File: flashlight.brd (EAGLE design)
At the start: 33.2 x 17.8 mm, 2 parts, among them IC1 AMC7135SOT-89

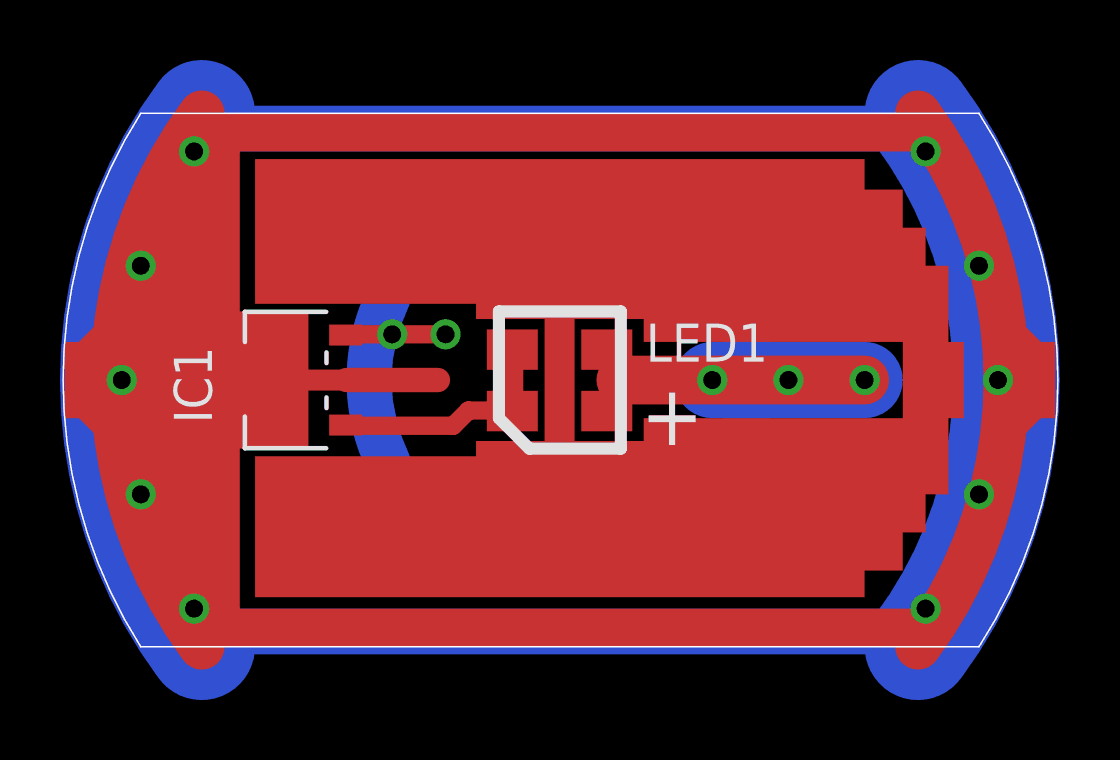
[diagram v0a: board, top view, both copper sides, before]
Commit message: add stockton logo to solder mask
add thermal mask to top
replace rhs of top with curved wire

label pins of switch on bottom
reduce size of tab solder area
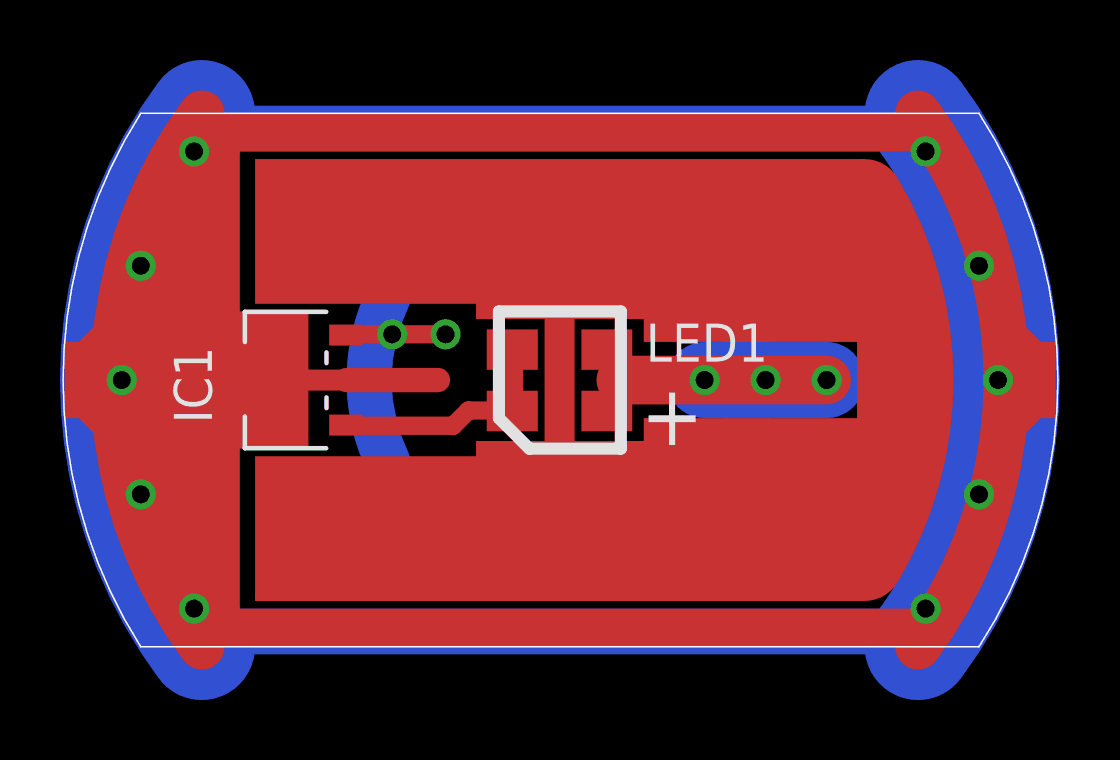
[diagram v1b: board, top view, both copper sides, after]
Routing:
- net N$22: track 0.00 -> 12.2 mm
- net N$14: track 13.2 -> 10.9 mm
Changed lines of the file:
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@@
 <rectangle x1="26.67" y1="2.54" x2="27.94" y2="7.62" layer="1"/>
 <rectangle x1="26.67" y1="10.16" x2="27.94" y2="15.24" layer="1"/>
-<rectangle x1="27.94" y1="5.08" x2="29.464" y2="12.7" layer="1"/>
-<rectangle x1="27.94" y1="3.81" x2="28.702" y2="5.08" layer="1"/>
-<rectangle x1="27.94" y1="12.7" x2="28.702" y2="13.97" layer="1"/>
-<rectangle x1="29.464" y1="7.62" x2="29.972" y2="10.16" layer="1"/>
 <wire x1="14.478" y1="11.176" x2="18.542" y2="11.176" width="0.4064" layer="25"/>
 <wire x1="18.542" y1="11.176" x2="18.542" y2="6.604" width="0.4064" layer="25"/>
@@
 <rectangle x1="13.716" y1="6.35" x2="16.002" y2="6.858" layer="1"/>
 <rectangle x1="5.08" y1="7.874" x2="5.334" y2="9.906" layer="29"/>
+<wire x1="23.876" y1="15.748" x2="26.924" y2="15.748" width="0.4064" layer="29" curve="-24.775141"/>
+<wire x1="24.638" y1="14.478" x2="24.638" y2="13.462" width="0.4064" layer="29"/>
+<wire x1="24.638" y1="14.478" x2="23.876" y2="15.24" width="0.4064" layer="29"/>
+<wire x1="24.638" y1="14.478" x2="25.4" y2="15.24" width="0.4064" layer="29"/>
+<wire x1="26.162" y1="14.478" x2="25.4" y2="15.24" width="0.4064" layer="29"/>
+<wire x1="26.162" y1="14.478" x2="26.924" y2="15.24" width="0.4064" layer="29"/>
+<wire x1="26.162" y1="14.478" x2="26.162" y2="13.462" width="0.4064" layer="29"/>
+<wire x1="24.638" y1="14.478" x2="24.638" y2="15.24" width="0.4064" layer="29"/>
+<wire x1="26.162" y1="14.478" x2="26.162" y2="15.24" width="0.4064" layer="29"/>
+<rectangle x1="6.35" y1="11.43" x2="8.89" y2="16.256" layer="29"/>
+<rectangle x1="6.35" y1="1.524" x2="8.89" y2="6.35" layer="29"/>
+<rectangle x1="24.384" y1="1.524" x2="26.67" y2="7.62" layer="29"/>
+<rectangle x1="24.384" y1="10.16" x2="26.67" y2="12.7" layer="29"/>
+<rectangle x1="3.556" y1="10.668" x2="5.842" y2="15.24" layer="29"/>
+<rectangle x1="3.556" y1="2.54" x2="5.842" y2="7.112" layer="29"/>
+<rectangle x1="6.35" y1="1.524" x2="26.67" y2="1.778" layer="1"/>
+<rectangle x1="26.416" y1="7.62" x2="27.94" y2="10.16" layer="1"/>
 </plain>
 <attributes>
@@
 </signal>
 <signal name="N$13">
-<via x="24.13" y="8.89" extent="1-16" drill="0.6"/>
+<via x="23.368" y="8.89" extent="1-16" drill="0.6"/>
 </signal>
 <signal name="N$14">
-<via x="21.59" y="8.89" extent="1-16" drill="0.6"/>
-<via x="26.67" y="8.89" extent="1-16" drill="0.6"/>
-<wire x1="26.67" y1="8.89" x2="18.542" y2="8.89" width="1.6256" layer="1"/>
-<wire x1="26.67" y1="8.89" x2="21.59" y2="8.89" width="2.54" layer="16"/>
+<via x="21.336" y="8.89" extent="1-16" drill="0.6"/>
+<via x="25.4" y="8.89" extent="1-16" drill="0.6"/>
+<wire x1="25.4" y1="8.89" x2="18.542" y2="8.89" width="1.6256" layer="1"/>
+<wire x1="25.4" y1="8.89" x2="21.336" y2="8.89" width="2.54" layer="16"/>
 </signal>
 <signal name="N$15">
@@
 <wire x1="9.398" y1="8.89" x2="12.446" y2="8.89" width="0.8128" layer="1"/>
 </signal>
+<signal name="N$22">
+<wire x1="26.67" y1="14.986" x2="26.67" y2="2.794" width="2.54" layer="1" curve="-62"/>
+</signal>
 </signals>
